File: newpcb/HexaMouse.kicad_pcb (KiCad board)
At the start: 2 copper layers, 21 x 17.8 mm, 23 parts, among them J1 Conn_01x02_Pin, J2 Conn_01x02_Pin, SW1 SW_SPDT, SW2 SW_Push, SW3 SW_Push, U1 XIAO-Add-On, U2 MLX90393SLW-ABA-011-RE, U3 MLX90393SLW-ABA-011-RE, U4 MLX90393SLW-ABA-011-RE

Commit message: Basic pcb design start
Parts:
- U1: moved to B.Cu
- moved U1 111.6 mm to (150.0, 75.0), turned to 90 degrees
- moved SW1 97.6 mm to (150.0, 66.5), turned to 180 degrees
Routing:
- added copper zone on B.Cu, net GND
- added copper zone on F.Cu, net GND
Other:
- board size 21 x 17.8 mm -> 56 x 63.5 mm

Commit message: Positioned mounting holes
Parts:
- moved H3 150.9 mm to (163.9, 108.0)
- moved SW2 135.8 mm to (176.0, 100.0), turned to -90 degrees
- moved H1 135.0 mm to (150.0, 84.0)
- moved H2 130.5 mm to (136.1, 108.0)
- moved U3 126.6 mm to (165.8, 90.8)
- moved U4 121.4 mm to (150.0, 118.3)
- moved J2 107.3 mm to (163.0, 79.0)
- moved D1 103.7 mm to (112.7, 120.8)
- moved D2 103.7 mm to (112.7, 127.5)
- moved D3 103.7 mm to (112.7, 134.1)
- moved U2 98.9 mm to (134.2, 90.8)
- moved SW3 87.3 mm to (124.0, 100.0), turned to 90 degrees
- moved J1 87.1 mm to (137.0, 79.0)
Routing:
- net GND: vias 0 -> 12

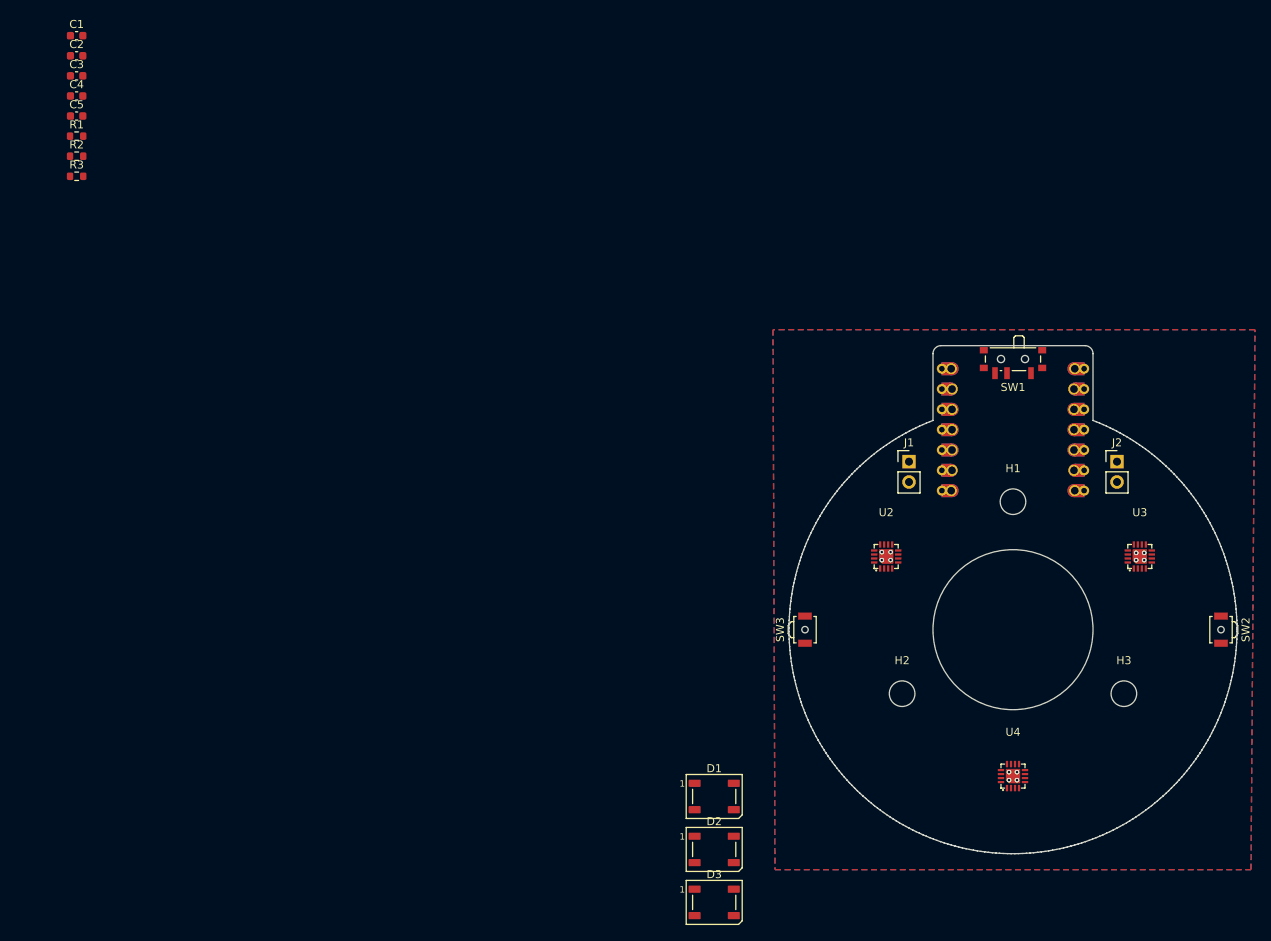
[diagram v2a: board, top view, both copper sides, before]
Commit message: Positioned LEDs
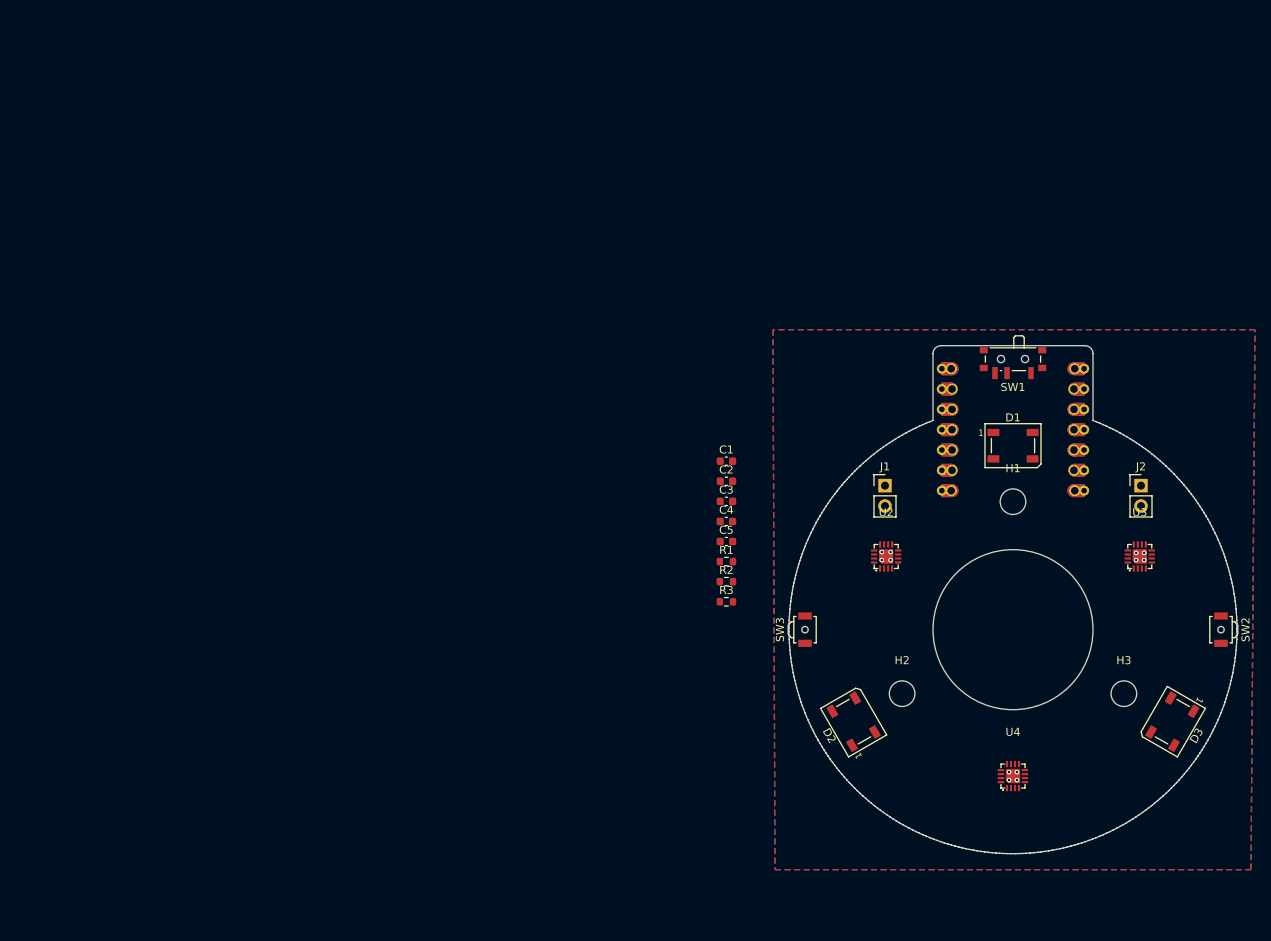
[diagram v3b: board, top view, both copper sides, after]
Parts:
- moved C1 97.1 mm to (114.2, 78.9)
- moved C2 97.1 mm to (114.2, 81.5)
- moved C4 97.1 mm to (114.2, 86.5)
- moved C5 97.1 mm to (114.2, 89.0)
- moved R2 97.1 mm to (114.2, 94.0)
- moved R3 97.1 mm to (114.2, 96.5)
- moved C3 97.1 mm to (114.2, 84.0)
- moved R1 97.1 mm to (114.2, 91.5)
- moved D3 61.6 mm to (169.9, 111.5), turned to -120 degrees
- moved D1 57.6 mm to (150.0, 77.0)
- moved D2 23.6 mm to (130.1, 111.5), turned to 120 degrees
- moved J1 4.24 mm to (134.0, 82.0)
- moved J2 4.24 mm to (166.0, 82.0)

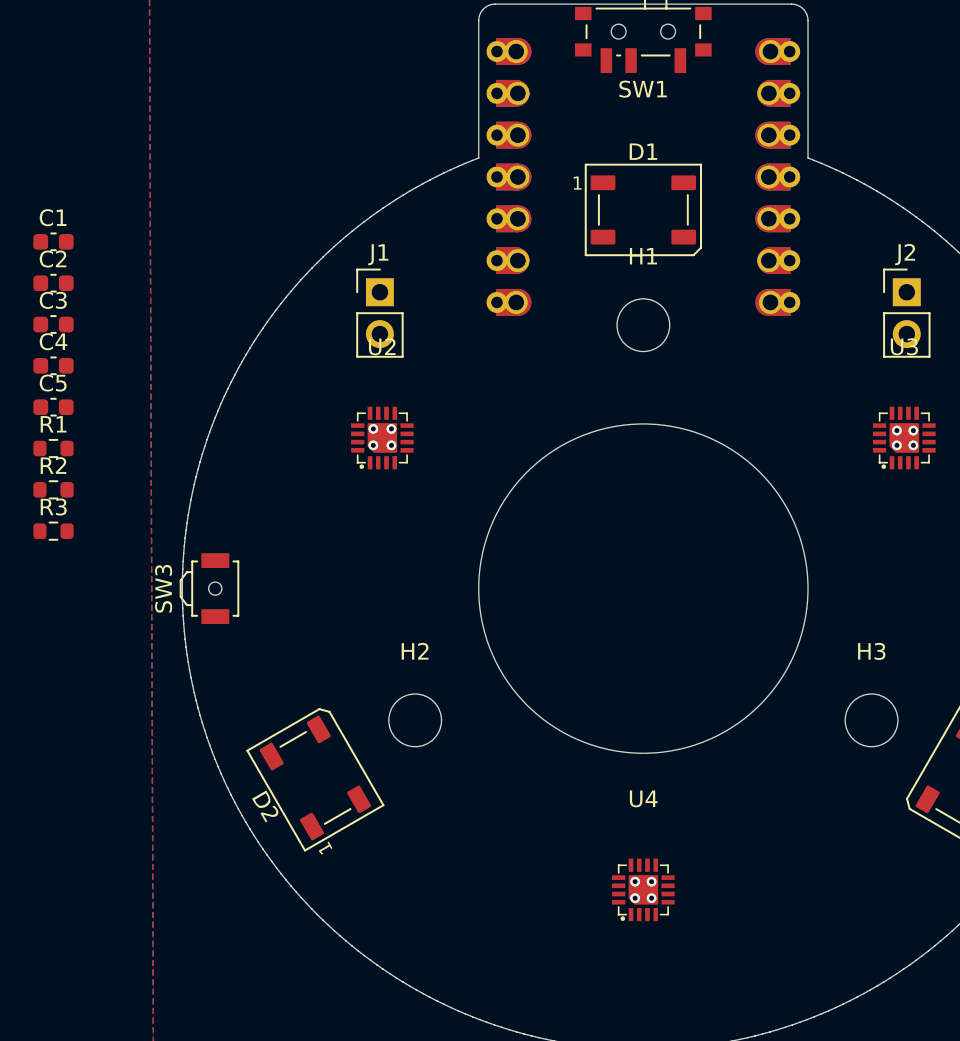
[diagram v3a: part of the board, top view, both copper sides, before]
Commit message: Positioned Capacitors
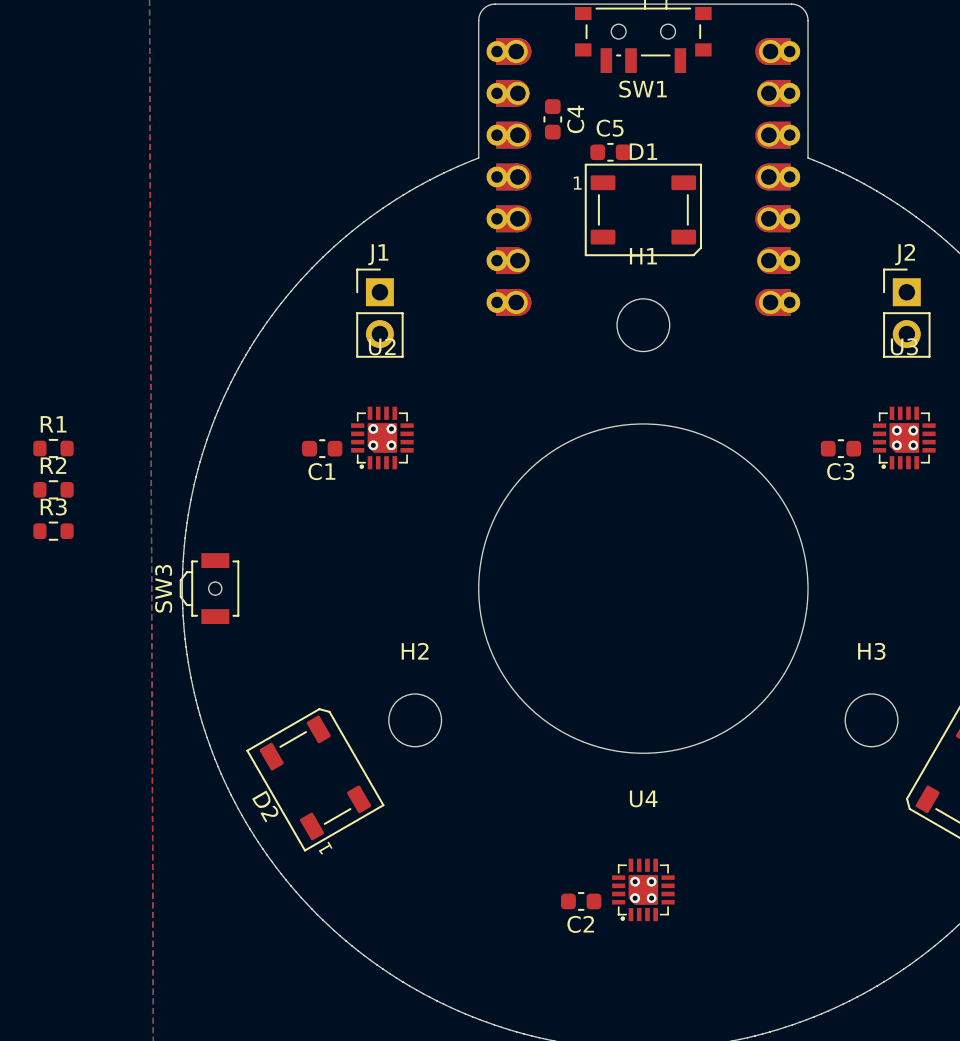
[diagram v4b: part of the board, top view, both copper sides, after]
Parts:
- moved C2 49.4 mm to (146.2, 119.0), turned to 180 degrees
- moved C3 48.4 mm to (162.0, 91.5), turned to 180 degrees
- moved C5 37.2 mm to (148.0, 73.5)
- moved C4 33.8 mm to (144.5, 71.5), turned to -90 degrees
- moved C1 20.6 mm to (130.5, 91.5), turned to 180 degrees
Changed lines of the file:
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@@
 	(footprint "Capacitor_SMD:C_0603_1608Metric"
 		(layer "F.Cu")
-		(at 114.175 78.94)
+		(at 130.5 91.5 180)
 		(descr "Capacitor SMD 0603 (1608 Metric), square (rectangular) end terminal, IPC-7351 nominal, (Body size source: IPC-SM-782 page 76, https://www.pcb-3d.com/wordpress/wp-content/uploads/ipc-sm-782a_amendment_1_and_2.pdf)")
 		(tags "capacitor")
@@
 		)
 		(property "LCSC" "C14663"
-			(at 0 0 0)
+			(at 0 0 180)
 			(unlocked yes)
 			(layer "F.Fab")
@@
 		(duplicate_pad_numbers_are_jumpers no)
 		(fp_line
+			(start -0.14058 0.51)
+			(end 0.14058 0.51)
+			(stroke
+				(width 0.12)
+				(type solid)
+			)
+			(layer "F.SilkS")
+		)
+		(fp_line
 			(start -0.14058 -0.51)
 			(end 0.14058 -0.51)
-			(stroke
-				(width 0.12)
-				(type solid)
-			)
-			(layer "F.SilkS")
-		)
-		(fp_line
-			(start -0.14058 0.51)
-			(end 0.14058 0.51)
 			(stroke
 				(width 0.12)
@@
 		)
 		(pad "1" smd roundrect
-			(at -0.775 0)
+			(at -0.775 0 180)
 			(size 0.9 0.95)
 			(layers "F.Cu" "F.Mask" "F.Paste")
@@
 		)
 		(pad "2" smd roundrect
-			(at 0.775 0)
+			(at 0.775 0 180)
 			(size 0.9 0.95)
 			(layers "F.Cu" "F.Mask" "F.Paste")
@@
 	(footprint "Capacitor_SMD:C_0603_1608Metric"
 		(layer "F.Cu")
-		(at 114.175 88.98)
+		(at 148 73.5)
 		(descr "Capacitor SMD 0603 (1608 Metric), square (rectangular) end terminal, IPC-7351 nominal, (Body size source: IPC-SM-782 page 76, https://www.pcb-3d.com/wordpress/wp-content/uploads/ipc-sm-782a_amendment_1_and_2.pdf)")
 		(tags "capacitor")
@@
 	(footprint "Capacitor_SMD:C_0603_1608Metric"
 		(layer "F.Cu")
-		(at 114.175 86.47)
+		(at 144.5 71.5 -90)
 		(descr "Capacitor SMD 0603 (1608 Metric), square (rectangular) end terminal, IPC-7351 nominal, (Body size source: IPC-SM-782 page 76, https://www.pcb-3d.com/wordpress/wp-content/uploads/ipc-sm-782a_amendment_1_and_2.pdf)")
 		(tags "capacitor")
 		(property "Reference" "C4"
-			(at 0 -1.43 0)
+			(at 0 -1.43 90)
 			(layer "F.SilkS")
 			(effects
@@
 		)
 		(property "Value" "10uF"
-			(at 0 1.43 0)
+			(at 0 1.43 90)
 			(layer "F.Fab")
 			(effects
@@
 		)
 		(property "Datasheet" ""
-			(at 0 0 0)
+			(at 0 0 90)
 			(layer "F.Fab")
 			(hide yes)
@@
 		)
 		(property "Description" "Unpolarized capacitor"
-			(at 0 0 0)
+			(at 0 0 90)
 			(layer "F.Fab")
 			(hide yes)
@@
 		)
 		(property "KiLib_Generator" "SMD_2terminal_chip_molded"
-			(at 0 0 0)
+			(at 0 0 90)
 			(layer "F.SilkS")
 			(hide yes)
@@
 		)
 		(property "LCSC" "C96446"
-			(at 0 0 0)
+			(at 0 0 270)
 			(unlocked yes)
 			(layer "F.Fab")
@@
 		(duplicate_pad_numbers_are_jumpers no)
 		(fp_line
+			(start -0.14058 0.51)
+			(end 0.14058 0.51)
+			(stroke
+				(width 0.12)
+				(type solid)
+			)
+			(layer "F.SilkS")
+		)
+		(fp_line
 			(start -0.14058 -0.51)
 			(end 0.14058 -0.51)
-			(stroke
-				(width 0.12)
-				(type solid)
-			)
-			(layer "F.SilkS")
-		)
-		(fp_line
-			(start -0.14058 0.51)
-			(end 0.14058 0.51)
 			(stroke
 				(width 0.12)
@@
 		)
 		(fp_text user "${REFERENCE}"
-			(at 0 0 0)
+			(at 0 0 90)
 			(layer "F.Fab")
 			(effects
@@
 		)
 		(pad "1" smd roundrect
-			(at -0.775 0)
+			(at -0.775 0 270)
 			(size 0.9 0.95)
 			(layers "F.Cu" "F.Mask" "F.Paste")
@@
 		)
 		(pad "2" smd roundrect
-			(at 0.775 0)
+			(at 0.775 0 270)
 			(size 0.9 0.95)
 			(layers "F.Cu" "F.Mask" "F.Paste")
@@
 	(footprint "Capacitor_SMD:C_0603_1608Metric"
 		(layer "F.Cu")
-		(at 114.175 83.96)
+		(at 162 91.5 180)
 		(descr "Capacitor SMD 0603 (1608 Metric), square (rectangular) end terminal, IPC-7351 nominal, (Body size source: IPC-SM-782 page 76, https://www.pcb-3d.com/wordpress/wp-content/uploads/ipc-sm-782a_amendment_1_and_2.pdf)")
 		(tags "capacitor")
@@
 		)
 		(property "LCSC" "C14663"
-			(at 0 0 0)
+			(at 0 0 180)
 			(unlocked yes)
 			(layer "F.Fab")
@@
 		(duplicate_pad_numbers_are_jumpers no)
 		(fp_line
+			(start -0.14058 0.51)
+			(end 0.14058 0.51)
+			(stroke
+				(width 0.12)
+				(type solid)
+			)
+			(layer "F.SilkS")
+		)
+		(fp_line
 			(start -0.14058 -0.51)
 			(end 0.14058 -0.51)
-			(stroke
-				(width 0.12)
-				(type solid)
-			)
-			(layer "F.SilkS")
-		)
-		(fp_line
-			(start -0.14058 0.51)
-			(end 0.14058 0.51)
 			(stroke
 				(width 0.12)
@@
 		)
 		(pad "1" smd roundrect
-			(at -0.775 0)
+			(at -0.775 0 180)
 			(size 0.9 0.95)
 			(layers "F.Cu" "F.Mask" "F.Paste")
@@
 		)
 		(pad "2" smd roundrect
-			(at 0.775 0)
+			(at 0.775 0 180)
 			(size 0.9 0.95)
 			(layers "F.Cu" "F.Mask" "F.Paste")
@@
 	(footprint "Capacitor_SMD:C_0603_1608Metric"
 		(layer "F.Cu")
-		(at 114.175 81.45)
+		(at 146.225 119 180)
 		(descr "Capacitor SMD 0603 (1608 Metric), square (rectangular) end terminal, IPC-7351 nominal, (Body size source: IPC-SM-782 page 76, https://www.pcb-3d.com/wordpress/wp-content/uploads/ipc-sm-782a_amendment_1_and_2.pdf)")
 		(tags "capacitor")
@@
 		)
 		(property "LCSC" "C14663"
-			(at 0 0 0)
+			(at 0 0 180)
 			(unlocked yes)
 			(layer "F.Fab")
@@
 		(duplicate_pad_numbers_are_jumpers no)
 		(fp_line
+			(start -0.14058 0.51)
+			(end 0.14058 0.51)
+			(stroke
+				(width 0.12)
+				(type solid)
+			)
+			(layer "F.SilkS")
+		)
+		(fp_line
 			(start -0.14058 -0.51)
 			(end 0.14058 -0.51)
-			(stroke
-				(width 0.12)
-				(type solid)
-			)
-			(layer "F.SilkS")
-		)
-		(fp_line
-			(start -0.14058 0.51)
-			(end 0.14058 0.51)
 			(stroke
 				(width 0.12)
@@
 		)
 		(pad "1" smd roundrect
-			(at -0.775 0)
+			(at -0.775 0 180)
 			(size 0.9 0.95)
 			(layers "F.Cu" "F.Mask" "F.Paste")
@@
 		)
 		(pad "2" smd roundrect
-			(at 0.775 0)
+			(at 0.775 0 180)
 			(size 0.9 0.95)
 			(layers "F.Cu" "F.Mask" "F.Paste")

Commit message: Resistor Positioning
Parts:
- moved R3 45.2 mm to (152.5, 72.5), turned to -90 degrees
- moved R1 43.3 mm to (155.5, 78.5), turned to -90 degrees
- moved R2 43.2 mm to (155.5, 81.5), turned to 90 degrees
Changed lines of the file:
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@@
 	(footprint "Resistor_SMD:R_0603_1608Metric"
 		(layer "F.Cu")
-		(at 114.175 96.51)
+		(at 152.5 72.5 -90)
 		(descr "Resistor SMD 0603 (1608 Metric), square (rectangular) end terminal, IPC-7351 nominal, (Body size source: IPC-SM-782 page 72, https://www.pcb-3d.com/wordpress/wp-content/uploads/ipc-sm-782a_amendment_1_and_2.pdf)")
 		(tags "resistor")
 		(property "Reference" "R3"
-			(at 0 -1.43 0)
+			(at 0 -1.43 90)
 			(layer "F.SilkS")
 			(effects
@@
 		)
 		(property "Value" "47o"
-			(at 0 1.43 0)
+			(at 0 1.43 90)
 			(layer "F.Fab")
 			(effects
@@
 		)
 		(property "Datasheet" ""
-			(at 0 0 0)
+			(at 0 0 90)
 			(layer "F.Fab")
 			(hide yes)
@@
 		)
 		(property "Description" "Resistor"
-			(at 0 0 0)
+			(at 0 0 90)
 			(layer "F.Fab")
 			(hide yes)
@@
 		)
 		(property "KiLib_Generator" "SMD_2terminal_chip_molded"
-			(at 0 0 0)
+			(at 0 0 90)
 			(layer "F.SilkS")
 			(hide yes)
@@
 		)
 		(property "LCSC" "C23182"
-			(at 0 0 0)
+			(at 0 0 270)
 			(unlocked yes)
 			(layer "F.Fab")
@@
 		(duplicate_pad_numbers_are_jumpers no)
 		(fp_line
+			(start -0.237258 0.5225)
+			(end 0.237258 0.5225)
+			(stroke
+				(width 0.12)
+				(type solid)
+			)
+			(layer "F.SilkS")
+		)
+		(fp_line
 			(start -0.237258 -0.5225)
 			(end 0.237258 -0.5225)
-			(stroke
-				(width 0.12)
-				(type solid)
-			)
-			(layer "F.SilkS")
-		)
-		(fp_line
-			(start -0.237258 0.5225)
-			(end 0.237258 0.5225)
 			(stroke
 				(width 0.12)
@@
 		)
 		(fp_text user "${REFERENCE}"
-			(at 0 0 0)
+			(at 0 0 90)
 			(layer "F.Fab")
 			(effects
@@
 		)
 		(pad "1" smd roundrect
-			(at -0.825 0)
+			(at -0.825 0 270)
 			(size 0.8 0.95)
 			(layers "F.Cu" "F.Mask" "F.Paste")
@@
 		)
 		(pad "2" smd roundrect
-			(at 0.825 0)
+			(at 0.825 0 270)
 			(size 0.8 0.95)
 			(layers "F.Cu" "F.Mask" "F.Paste")
@@
 	(footprint "Resistor_SMD:R_0603_1608Metric"
 		(layer "F.Cu")
-		(at 114.175 94)
+		(at 155.5 81.5 90)
 		(descr "Resistor SMD 0603 (1608 Metric), square (rectangular) end terminal, IPC-7351 nominal, (Body size source: IPC-SM-782 page 72, https://www.pcb-3d.com/wordpress/wp-content/uploads/ipc-sm-782a_amendment_1_and_2.pdf)")
 		(tags "resistor")
 		(property "Reference" "R2"
-			(at 0 -1.43 0)
+			(at 0 -1.43 90)
 			(layer "F.SilkS")
 			(effects
@@
 		)
 		(property "Value" "10kO"
-			(at 0 1.43 0)
+			(at 0 1.43 90)
 			(layer "F.Fab")
 			(effects
@@
 		)
 		(property "Datasheet" ""
-			(at 0 0 0)
+			(at 0 0 90)
 			(layer "F.Fab")
 			(hide yes)
@@
 		)
 		(property "Description" "Resistor"
-			(at 0 0 0)
+			(at 0 0 90)
 			(layer "F.Fab")
 			(hide yes)
@@
 		)
 		(property "KiLib_Generator" "SMD_2terminal_chip_molded"
-			(at 0 0 0)
+			(at 0 0 90)
 			(layer "F.SilkS")
 			(hide yes)
@@
 		)
 		(property "LCSC" "C25804"
-			(at 0 0 0)
+			(at 0 0 90)
 			(unlocked yes)
 			(layer "F.Fab")
@@
 		)
 		(fp_text user "${REFERENCE}"
-			(at 0 0 0)
+			(at 0 0 90)
 			(layer "F.Fab")
 			(effects
@@
 		)
 		(pad "1" smd roundrect
-			(at -0.825 0)
+			(at -0.825 0 90)
 			(size 0.8 0.95)
 			(layers "F.Cu" "F.Mask" "F.Paste")
@@
 		)
 		(pad "2" smd roundrect
-			(at 0.825 0)
+			(at 0.825 0 90)
 			(size 0.8 0.95)
 			(layers "F.Cu" "F.Mask" "F.Paste")
@@
 	(footprint "Resistor_SMD:R_0603_1608Metric"
 		(layer "F.Cu")
-		(at 114.175 91.49)
+		(at 155.5 78.5 -90)
 		(descr "Resistor SMD 0603 (1608 Metric), square (rectangular) end terminal, IPC-7351 nominal, (Body size source: IPC-SM-782 page 72, https://www.pcb-3d.com/wordpress/wp-content/uploads/ipc-sm-782a_amendment_1_and_2.pdf)")
 		(tags "resistor")
 		(property "Reference" "R1"
-			(at 0 -1.43 0)
+			(at 0 -1.43 90)
 			(layer "F.SilkS")
 			(effects
@@
 		)
 		(property "Value" "10kO"
-			(at 0 1.43 0)
+			(at 0 1.43 90)
 			(layer "F.Fab")
 			(effects
@@
 		)
 		(property "Datasheet" ""
-			(at 0 0 0)
+			(at 0 0 90)
 			(layer "F.Fab")
 			(hide yes)
@@
 		)
 		(property "Description" "Resistor"
-			(at 0 0 0)
+			(at 0 0 90)
 			(layer "F.Fab")
 			(hide yes)
@@
 		)
 		(property "KiLib_Generator" "SMD_2terminal_chip_molded"
-			(at 0 0 0)
+			(at 0 0 90)
 			(layer "F.SilkS")
 			(hide yes)
@@
 		)
 		(property "LCSC" "C25804"
-			(at 0 0 0)
+			(at 0 0 270)
 			(unlocked yes)
 			(layer "F.Fab")
@@
 		(duplicate_pad_numbers_are_jumpers no)
 		(fp_line
+			(start -0.237258 0.5225)
+			(end 0.237258 0.5225)
+			(stroke
+				(width 0.12)
+				(type solid)
+			)
+			(layer "F.SilkS")
+		)
+		(fp_line
 			(start -0.237258 -0.5225)
 			(end 0.237258 -0.5225)
-			(stroke
-				(width 0.12)
-				(type solid)
-			)
-			(layer "F.SilkS")
-		)
-		(fp_line
-			(start -0.237258 0.5225)
-			(end 0.237258 0.5225)
 			(stroke
 				(width 0.12)
@@
 		)
 		(fp_text user "${REFERENCE}"
-			(at 0 0 0)
+			(at 0 0 90)
 			(layer "F.Fab")
 			(effects
@@
 		)
 		(pad "1" smd roundrect
-			(at -0.825 0)
+			(at -0.825 0 270)
 			(size 0.8 0.95)
 			(layers "F.Cu" "F.Mask" "F.Paste")
@@
 		)
 		(pad "2" smd roundrect
-			(at 0.825 0)
+			(at 0.825 0 270)
 			(size 0.8 0.95)
 			(layers "F.Cu" "F.Mask" "F.Paste")
